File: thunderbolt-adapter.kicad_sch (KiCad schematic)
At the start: 99 parts, among them J1 DX07S024JJ2R1300, J2 PCIe_x4_Conn_EdgeMount, U1 SI52112-B6-GT, U2 AP62301WU-7, U3 TPS65983BAZBHR, U4 JHL6340SLLSQ, U5 MX25L8006EM1I-12G, Y1 25MHz

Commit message: Connect TPS65983 (WiP)
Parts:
- added R? (x5): R_100k_0402, antmicro-footprints:0402-res, symbol antmicroResistors0402:R_100k_0402
- added R? (x4): R_10k_0402, antmicro-footprints:0402-res, symbol antmicroResistors0402:R_10k_0402
- added R?: R_1M0_0402, antmicro-footprints:0402-res, symbol antmicroResistors0402:R_1M0_0402
- added R?: R_0R_0402, antmicro-footprints:0402-res, symbol antmicroResistors0402:R_0R_0402
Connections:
- net 3V3_SYS: now also R?.2
- net GND: now also R?.1, R?.1, R?.1, R?.2
- net TPS_3V3: now also R?.1, R?.1, R?.1, R?.1, R?.1
- net USB_T_P: now reaches J1.A6
- net USB_T_P: now also U3.K6 (C_USB_TP)
- net USB_T_N: now reaches J1.A7
- net USB_T_N: now also U3.L6 (C_USB_TN)
- net SBU1: now reaches J1.A8
- net SBU1: now also U3.K8 (C_SBU1)
- net USB_B_P: now reaches J1.B6
- net USB_B_P: now also U3.K7 (C_USB_BP)
- net USB_B_N: now reaches J1.B7
- net USB_B_N: now also U3.L7 (C_USB_BN)
- net SBU2: now reaches J1.B8
- net SBU2: now also U3.L8 (C_SBU2)
- net at U3.C10 (GPIO4(HPD_TXRX)): now also R?.2
- net at U3.D5 (DEBUG_CTL2(GPIO17,_I2CADDR_B5)): now also R?.2
- net at U3.D6 (HRESET): now also R?.2
- net at U3.D7 (GPIO7): now also R?.2
- net at U3.E11 (MRESET(GPIO11)): now also R?.1
- net at U3.E2 (UART_TX): now also U3.F2 (UART_RX), R?.2
- net at U3.E4 (DEBUG_CTL1(GPIO16,_I2CADDR_B4)): now also R?.2
- net at U3.F10 (BUSPOWERZ(GPIO10)): now also R?.2
- net RESET_N: now reaches U3.F11 (RESETZ(GPIO9))
- net RESET_N: now also U4.F4 (RESET_N), R?.1
- net at U3.G10 (GPIO6): now also R?.2
- net HPD: now reaches U4.M4 (PA_DPSRC_HPD)
- net HPD: now also R?.1, R?.2

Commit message: Connect TPS65983 I2C
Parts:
- added R? (x2): R_10k_0402, antmicro-footprints:0402-res, symbol antmicroResistors0402:R_10k_0402
- added R? (x2): R_3k3_0402, antmicro-footprints:0402-res, symbol antmicroResistors0402:R_3k3_0402
- added R? (x2): R_2k2_0402, antmicro-footprints:0402-res, symbol antmicroResistors0402:R_2k2_0402
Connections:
- net 3V3_SYS: now also R?.2, R?.2, R?.2
- net TPS_3V3: now also R?.1, R?.1, R?.1
- net at U3.A5 (I2C_SDA2): now also R?.2
- net at U3.B5 (I2C_SCL2): now also R?.2
- net at U3.B6 (I2C_IRQ2Z): now also R?.2
- net I2C1_IRQ: now reaches U3.C1 (I2C_IRQ1Z)
- net I2C1_IRQ: now also U4.J4 (POC_GPIO_0), R?.1
- net I2C1_SDA: now reaches U3.D1 (I2C_SDA1)
- net I2C1_SDA: now also U4.U1 (GPIO_0), R?.1
- net I2C1_SCL: now reaches U3.D2 (I2C_SCL1)
- net I2C1_SCL: now also U4.U2 (GPIO_1), R?.1
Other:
- moved on the sheet: C4, C6, C7, C8, C?, J1

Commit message: Connect SPI flash memory
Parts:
- added R? (x4): R_3k3_0402, antmicro-footprints:0402-res, symbol antmicroResistors0402:R_3k3_0402
- added R?: R_10k_0402, antmicro-footprints:0402-res, symbol antmicroResistors0402:R_10k_0402
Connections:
- net 3V3_SYS: now also R?.2, R?.2, R?.2, R?.2
- net TPS_3V3: now also R?.1
- net SPI_SCLK: now reaches U3.A3 (SPI_CLK)
- net SPI_SCLK: now also U4.AB4 (EE_CLK), U5.6 (SCLK)
- net SPI_MISO: now reaches U3.A4 (SPI_POCI)
- net SPI_MISO: now also U4.AC4 (EE_D0), U5.2 (SO/IO1), R?.1
- net at U3.B2 (GPIO0(HD3_AMSEL)): now also R?.2
- net SPI_CS: now reaches U3.B3 (SPI_CSZ)
- net SPI_CS: now also U4.AC3 (EE_CS_N), U5.1 (~{CS}), R?.1
- net SPI_MOSI: now reaches U3.B4 (SPI_PICO)
- net SPI_MOSI: now also U4.AB3 (EE_DI), U5.5 (SI/IO0)
- net FLASH_WP: now reaches U4.V1 (GPIO_2)
- net FLASH_WP: now also U5.3 (~{WP}), R?.1
- net at U5.7 (~{HOLD}): now also R?.1
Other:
- moved on the sheet: C?, U5, Y?

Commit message: Finish connecting TPS65983
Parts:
- added R? (x2): R_1M0_0402, antmicro-footprints:0402-res, symbol antmicroResistors0402:R_1M0_0402
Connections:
- net GND: now also R?.1, R?.1
- net LSX_P2R: now reaches U3.K4 (LSX_P2R)
- net LSX_P2R: now also U4.A4 (PA_LSRX), R?.2
- net USB_RP_N: now reaches U3.K5 (USB_RP_N)
- net USB_RP_N: now also U4.D20 (PA_USB2_D_N)
- net LSX_R2P: now reaches U3.L4 (LSX_R2P)
- net LSX_R2P: now also U4.A5 (PA_LSTX), R?.2
- net USB_RP_P: now reaches U3.L5 (USB_RP_P)
- net USB_RP_P: now also U4.E20 (PA_USB2_D_P)

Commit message: Connect JHL6340 power and signals (WiP)
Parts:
- removed C? (x2): C_10u_0402, antmicro-footprints:0402-cap, symbol antmicroCapacitors0402:C_10u_0402
- added C? (x7): C_10u_0402, antmicro-footprints:0402-cap, symbol antmicroCapacitors0402:C_10u_0402
- added C? (x6): C_100n_0402, antmicro-footprints:0402-cap, symbol antmicroCapacitors0402:C_100n_0402
- added C? (x4): C_1u_0402, antmicro-footprints:0402-cap, symbol antmicroCapacitors0402:C_1u_0402
- added L?: DFE18SBN1R0ME0L, antmicro-footprints:INDC1608X100N, symbol antmicroFixedInductors:DFE18SBN1R0ME0L
- added R? (x10): R_100k_0402, antmicro-footprints:0402-res, symbol antmicroResistors0402:R_100k_0402
- added R?: R_14k_0402, antmicro-footprints:0402-res, symbol antmicroResistors0402:R_14k_0402
- added R? (x10): R_10k_0402, antmicro-footprints:0402-res, symbol antmicroResistors0402:R_10k_0402
- added R? (x2): R_2k2_0402, antmicro-footprints:0402-res, symbol antmicroResistors0402:R_2k2_0402
- added R? (x3): R_1M0_0402, antmicro-footprints:0402-res, symbol antmicroResistors0402:R_1M0_0402
- added R? (x2): R_499R_0402, antmicro-footprints:0402-res, symbol antmicroResistors0402:R_499R_0402
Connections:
- net 3V3_SYS: now also U4.A2 (VCC3P3_SVR), U4.A3 (VCC3P3_SVR), U4.B3 (VCC3P3_SVR), U4.F8 (VCC3P3_SX), U4.H9 (VCC3P3A), C?.1, C?.1, C?.1, C?.1, C?.1, C?.1, C?.1, C?.2, C?.2, C?.2, C?.2, C?.2, L?.2, R?.1, R?.1, R?.2, R?.2, R?.2, R?.2, R?.2
- net GND: now also C?.1, C?.1, C?.1, C?.1, C?.1, C?.1, C?.1, C?.2, C?.2, C?.2, C?.2, C?.2, C?.2, C?.2, C?.2, C?.2, C?.2, R?.1, R?.1, R?.1, R?.2, R?.2, R?.2, R?.2, R?.2, R?.2, R?.2, R?.2, R?.2, R?.2, R?.2, R?.2, R?.2, R?.2, R?.2, R?.2, R?.2, R?.2
- net TPS_3V3: now also C?.1
- net PCIE_WAKE: now reaches J2.B11 (WAKE#)
- net PCIE_WAKE: now also U4.F2 (POC_GPIO_4), R?.2
- net at U4.AA1 (GPIO_8): now also R?.1
- net at U4.AA2 (DPSNK0_HPD): now also R?.1
- net at U4.AC5 (PCIE_CLKREQ_N): now also R?.2
- net at U4.B4 (PB_LSTX): now also R?.1
- net at U4.B5 (PB_LSRX): now also R?.1
- net at U4.D2 (POC_GPIO_5): now also R?.1
- net at U4.D4 (POC_GPIO_2): now also R?.1
- net at U4.E2 (POC_GPIO_1): now also R?.1
- net at U4.F1 (POC_GPIO_6): now also R?.1
- net at U4.F19 (PB_USB2_RBIAS): now also R?.1
- net at U4.G1 (DPSRC_HPD): now also R?.1
- net at U4.G2 (PB_DPSRC_HPD): now also R?.1
- net at U4.H19 (PA_USB2_RBIAS): now also R?.1
- net at U4.H4 (POC_GPIO_3): now also R?.1
- net at U4.N4 (DPSNK1_DDC_DATA): now also R?.2
- net at U4.T4 (TCK): now also R?.1
- net at U4.V2 (GPIO_3): now also R?.1
- net at U4.V4 (TMS): now also R?.1
- net at U4.W1 (GPIO_4): now also R?.1
- net at U4.W2 (GPIO_5): now also R?.1
- net at U4.W4 (TDO): now also R?.1
- net at U4.Y1 (GPIO_6): now also R?.1
- net at U4.Y18 (DPSNK_RBIAS): now also R?.2
- net at U4.Y2 (GPIO_7): now also R?.1
- net at U4.Y4 (TDI): now also R?.1
- net at U4.Y6 (DPSNK1_HPD): now also R?.1
- net at U4.Y8 (DPSNK1_DDC_CLK): now also R?.2
- net at U4.R13 (VCC3P3_S0): now also C?.1, C?.2, C?.2, L?.1
- net at U4.R6 (VCC3P3_LC): now also C?.1
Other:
- moved on the sheet: C12, C14, C17, C19, C22, R?, TP?

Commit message: Finish connecting JHL6340
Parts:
- added C? (x12): C_220n_0402, antmicro-footprints:0402-cap, symbol antmicroCapacitors0402:C_220n_0402
- added R? (x2): R_2k2_0402, antmicro-footprints:0402-res, symbol antmicroResistors0402:R_2k2_0402
- added R?: R_14k_0402, antmicro-footprints:0402-res, symbol antmicroResistors0402:R_14k_0402
- added R?: R_3k01_0402, antmicro-footprints:0402-res, symbol antmicroResistors0402:R_3k01_0402
- added R?: R_3k3_0402, antmicro-footprints:0402-res, symbol antmicroResistors0402:R_3k3_0402
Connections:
- net GND: now also R?.1, R?.1, R?.1, R?.1, R?.2
- net PCIE_CLK_CON_P: now reaches U1.5 (DIFF1)
- net PCIE_CLK_CON_P: now also J2.A13 (REFCLK+)
- net PCIE_CLK_CON_N: now reaches U1.6 (~{DIFF1})
- net PCIE_CLK_CON_N: now also J2.A14 (REFCLK-)
- net PCIE_CLK_JHL_P: now reaches U1.7 (DIFF2)
- net PCIE_CLK_JHL_P: now also U4.V19 (PCIE_REFCLK_100_IN_P)
- net PCIE_CLK_JHL_N: now reaches U1.8 (~{DIFF2})
- net PCIE_CLK_JHL_N: now also U4.T19 (PCIE_REFCLK_100_IN_N)
- net TB_RX1_N: now reaches J1.A10
- net TB_RX1_N: now also U4.B15 (PA_RX1_N)
- net TB_RX1_P: now reaches J1.A11
- net TB_RX1_P: now also U4.A15 (PA_RX1_P)
- net TB_TX0_P: now reaches J1.A2
- net TB_TX0_P: now also C?.1
- net TB_TX0_N: now reaches J1.A3
- net TB_TX0_N: now also C?.1
- net TB_RX0_N: now reaches J1.B10
- net TB_RX0_N: now also U4.A21 (PA_RX0_N)
- net TB_RX0_P: now reaches J1.B11
- net TB_RX0_P: now also U4.B21 (PA_RX0_P)
- net TB_TX1_P: now reaches J1.B2
- net TB_TX1_P: now also C?.1
- net TB_TX1_N: now reaches J1.B3
- net TB_TX1_N: now also C?.1
- net PCIE_PWRGD: now reaches J2.A11 (PWRGD)
- net PCIE_PWRGD: now also U4.L4 (PERST_N), R?.2
- net PCIE_RX0_P: now reaches J2.A16 (HSIp(0))
- net PCIE_RX0_P: now also U4.Y23 (PCIE_RX0_P)
- net PCIE_RX0_N: now reaches J2.A17 (HSIn(0))
- net PCIE_RX0_N: now also U4.Y22 (PCIE_RX0_N)
- net PCIE_RX1_P: now reaches J2.A21 (HSIp(1))
- net PCIE_RX1_P: now also U4.T23 (PCIE_RX1_P)
- net PCIE_RX1_N: now reaches J2.A22 (HSIn(1))
- net PCIE_RX1_N: now also U4.T22 (PCIE_RX1_N)
- net PCIE_RX2_P: now reaches J2.A25 (HSIp(2))
- net PCIE_RX2_P: now also U4.M23 (PCIE_RX2_P)
- net PCIE_RX2_N: now reaches J2.A26 (HSIn(2))
- net PCIE_RX2_N: now also U4.M22 (PCIE_RX2_N)
- net PCIE_RX3_P: now reaches J2.A29 (HSIp(3))
- net PCIE_RX3_P: now also U4.H23 (PCIE_RX3_P)
- net PCIE_RX3_N: now reaches J2.A30 (HSIn(3))
- net PCIE_RX3_N: now also U4.H22 (PCIE_RX3_N)
- net PCIE_TX0_P: now reaches J2.B14 (HSOp(0))
- net PCIE_TX0_P: now also C?.1
- net PCIE_TX0_N: now reaches J2.B15 (HSOn(0))
- net PCIE_TX0_N: now also C?.1
- net PCIE_TX1_P: now reaches J2.B19 (HSOp(1))
- net PCIE_TX1_P: now also C?.1
- net PCIE_TX1_N: now reaches J2.B20 (HSOn(1))
- net PCIE_TX1_N: now also C?.1
- net PCIE_TX2_P: now reaches J2.B23 (HSOp(2))
- net PCIE_TX2_P: now also C?.1
- net PCIE_TX2_N: now reaches J2.B24 (HSOn(2))
- net PCIE_TX2_N: now also C?.1
- net PCIE_TX3_P: now reaches J2.B27 (HSOp(3))
- net PCIE_TX3_P: now also C?.1
- net PCIE_TX3_N: now reaches J2.B28 (HSOn(3))
- net PCIE_TX3_N: now also C?.1
- net at U4.A17 (PA_TX1_P): now also C?.2
- net at U4.A19 (PA_TX0_P): now also C?.2
- net at U4.B17 (PA_TX1_N): now also C?.2
- net at U4.B19 (PA_TX0_N): now also C?.2
- net at U4.F22 (PCIE_TX3_N): now also C?.2
- net at U4.F23 (PCIE_TX3_P): now also C?.2
- net at U4.K22 (PCIE_TX2_N): now also C?.2
- net at U4.K23 (PCIE_TX2_P): now also C?.2
- net at U4.N16 (PCIE_RBIAS): now also R?.1
- net at U4.N6 (DPSRC_RBIAS): now also R?.2
- net at U4.P22 (PCIE_TX1_N): now also C?.2
- net at U4.P23 (PCIE_TX1_P): now also C?.2
- net at U4.V22 (PCIE_TX0_N): now also C?.2
- net at U4.V23 (PCIE_TX0_P): now also C?.2
- net at U4.Y5 (DPSNK0_DDC_CLK): now also R?.2
- new net: R?.2, U4.R4 (DPSNK0_DDC_DATA)

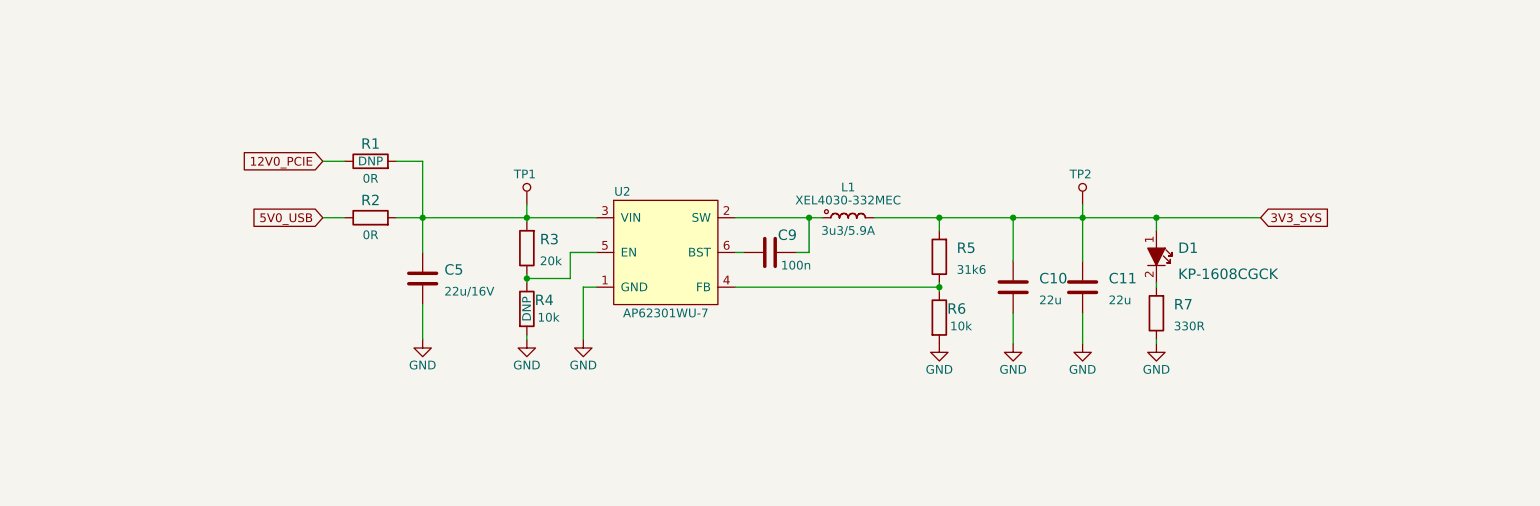
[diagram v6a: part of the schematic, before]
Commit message: Replace 3V3 SMPS
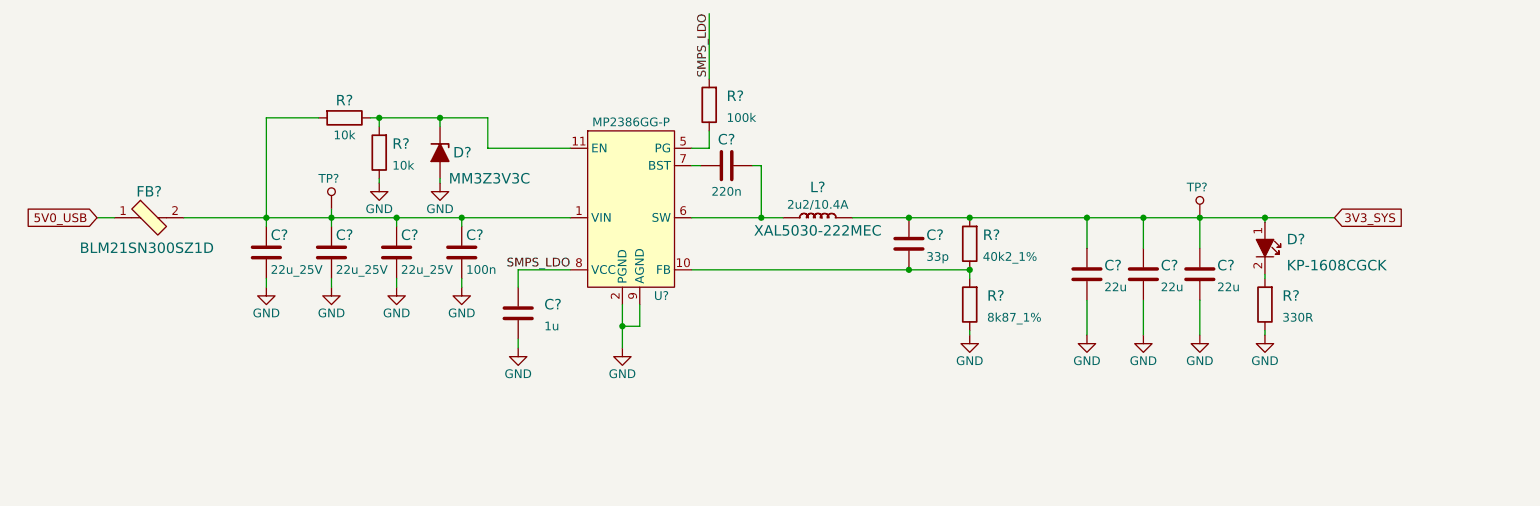
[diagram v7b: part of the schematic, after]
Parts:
- removed C10, C11: C_22u_0603, antmicro-footprints:0603-cap, symbol antmicroCapacitors0603:C_22u_0603
- removed C5: C_22u_0805_16V, antmicro-footprints:0805-cap, symbol antmicroCapacitorsmisc:C_22u_0805_16V
- removed C9: C_100n_0402, antmicro-footprints:0402-cap, symbol antmicroCapacitors0402:C_100n_0402
- removed D1: KP-1608CGCK, antmicro-footprints:LED_0603, symbol antmicroLEDIndicationDiscrete:KP-1608CGCK
- removed L1: XEL4030-332MEC, antmicro-footprints:Coilcraft-XEL4030, symbol antmicroFixedInductors:XEL4030-332MEC
- removed R1, R2: R_0R_1206, antmicro-footprints:1206-res, symbol antmicroResistorsmisc:R_0R_1206
- removed R3: R_20k_0402, antmicro-footprints:0402-res, symbol antmicroResistors0402:R_20k_0402
- removed R4, R6: R_10k_0402, antmicro-footprints:0402-res, symbol antmicroResistors0402:R_10k_0402
- removed R5: R_31k6_0402, antmicro-footprints:0402-res, symbol antmicroResistors0402:R_31k6_0402
- removed R7: R_330R_0402, antmicro-footprints:0402-res, symbol antmicroResistors0402:R_330R_0402
- removed TP1, TP2: TP_SMD1MM, antmicro-footprints:Testpoint_smd_1mm, symbol antmicroTestPoints:TP_SMD1MM
- removed U2: AP62301WU-7, antmicro-footprints:TSOT23-6, symbol antmicroDCDCConverters:AP62301WU-7
- added C? (x3): C_22u_0805_25V, antmicro-footprints:0805-cap, symbol antmicroCapacitorsmisc:C_22u_0805_25V
- added C? (x3): C_22u_0603, antmicro-footprints:0603-cap, symbol antmicroCapacitors0603:C_22u_0603
- added C?: C_220n_0402, antmicro-footprints:0402-cap, symbol antmicroCapacitors0402:C_220n_0402
- added C?: C_33p_0402, antmicro-footprints:0402-cap, symbol antmicroCapacitors0402:C_33p_0402
- added C?: C_100n_0402, antmicro-footprints:0402-cap, symbol antmicroCapacitors0402:C_100n_0402
- added C?: C_1u_0402, antmicro-footprints:0402-cap, symbol antmicroCapacitors0402:C_1u_0402
- added D?: MM3Z3V3C, antmicro-footprints:SOD-323F, symbol antmicroDiodesZenerSingle:MM3Z3V3C
- added D?: KP-1608CGCK, antmicro-footprints:LED_0603, symbol antmicroLEDIndicationDiscrete:KP-1608CGCK
- added FB?: BLM21SN300SZ1D, antmicro-footprints:0805-res, symbol antmicroFerriteBeadsandChips:BLM21SN300SZ1D
- added L?: XAL5030-222MEC, antmicro-footprints:Coilcraft-XAL5030, symbol antmicroFixedInductors:XAL5030-222MEC
- added R? (x2): R_10k_0402, antmicro-footprints:0402-res, symbol antmicroResistors0402:R_10k_0402
- added R?: R_100k_0402, antmicro-footprints:0402-res, symbol antmicroResistors0402:R_100k_0402
- added R?: R_40k2_1%_0402, antmicro-footprints:0402-res, symbol antmicroResistors0402:R_40k2_1%_0402
- added R?: R_8k87_1%_0402, antmicro-footprints:0402-res, symbol antmicroResistors0402:R_8k87_1%_0402
- added R?: R_330R_0402, antmicro-footprints:0402-res, symbol antmicroResistors0402:R_330R_0402
- added TP? (x2): TP_SMD1MM, antmicro-footprints:Testpoint_smd_1mm, symbol antmicroTestPoints:TP_SMD1MM
- added U?: MP2386GG-P, antmicro-footprints:QFN-11_2x2mm_P0.5mm, symbol antmicroDCDCConverters:MP2386GG-P
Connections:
- net 3V3_SYS: now also C?.2, C?.2, C?.2, C?.2, D?.1, L?.2 (P), R?.2, TP?.1
- net 5V0_USB: now also FB?.1
- net GND: now also C?.1, C?.1, C?.1, C?.2, C?.2, C?.2, C?.2, C?.2, D?.A, R?.1, R?.1, R?.1, U?.2 (PGND), U?.3 (PGND), U?.4 (PGND), U?.9 (AGND)
- new net: C?.1, C?.1, C?.1, C?.1, FB?.2, R?.2, TP?.1, U?.1 (VIN)
- new net: D?.K, R?.1, R?.2, U?.11 (EN)
- new net: C?.1, U?.7 (BST)
- new net: C?.2, L?.1 (P), U?.6 (SW)
- new net: C?.1, R?.1, R?.2, U?.10 (FB)
- new net: R?.1, U?.5 (PG)
- new net: D?.2, R?.2
- new net SMPS_LDO: C?.1, R?.2, U?.8 (VCC)
